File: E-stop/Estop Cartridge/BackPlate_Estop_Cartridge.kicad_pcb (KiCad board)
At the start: 2 copper layers, 83.3 x 41.9 mm, 8 parts, among them J1 EVM-915-DTS, P1 CONN_01X02, P2 CONN_01X02, P3 CONN_01X02, U1 Teensy_3.1

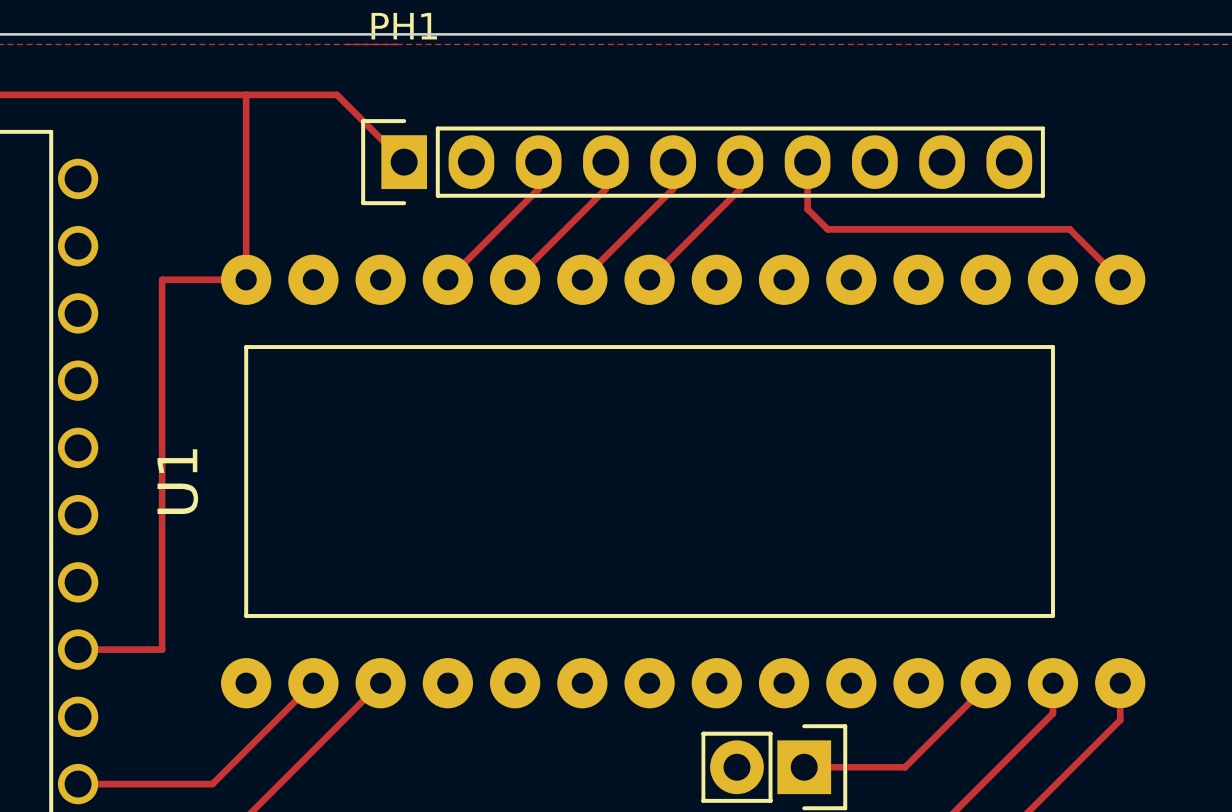
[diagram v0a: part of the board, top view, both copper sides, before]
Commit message: Updated to have Pin for Editing BreadBoard
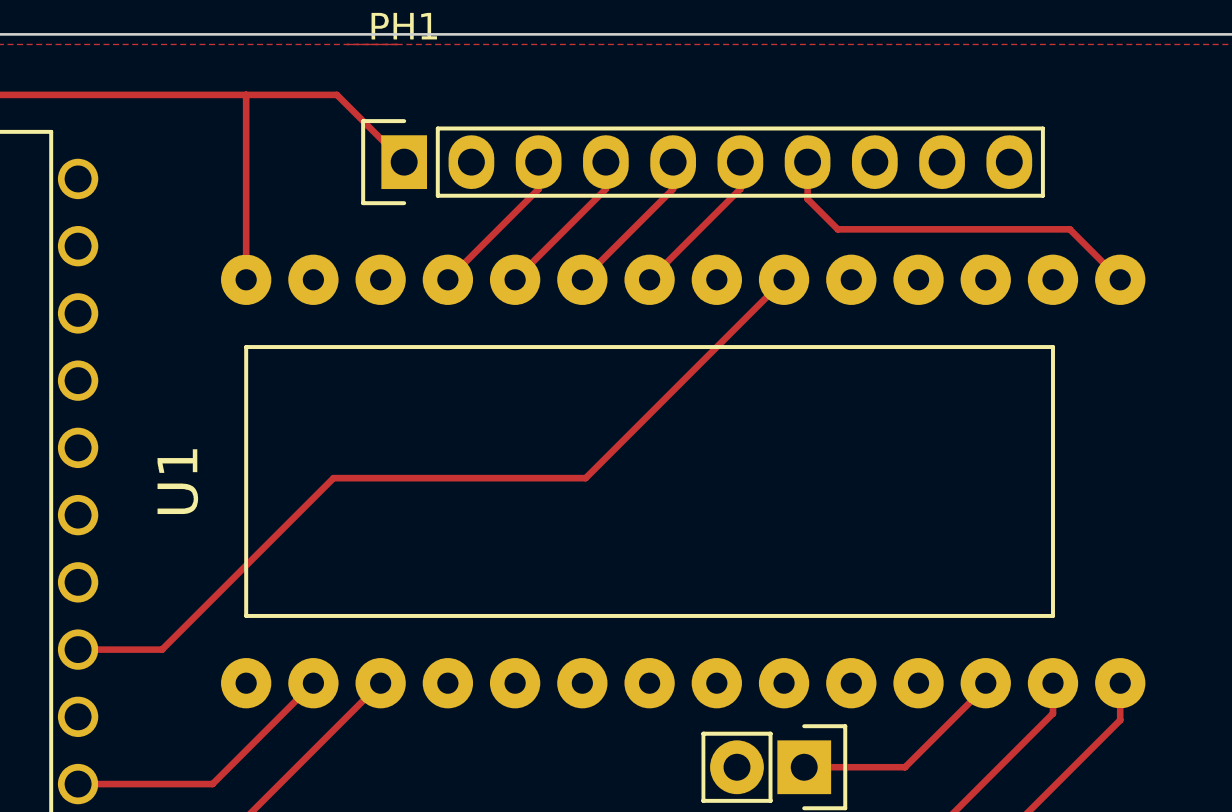
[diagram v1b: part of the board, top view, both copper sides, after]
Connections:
- J1 pad 5: +5V -> Net-(J1-Pad5)
- U1 pad 18: Net-(U1-Pad18) -> Net-(J1-Pad5)
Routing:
- net Net-(J1-Pad5): track 0.00 -> 32.5 mm
- net +5V: track 154.3 -> 134.0 mm
